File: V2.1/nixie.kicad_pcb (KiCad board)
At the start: 4 copper layers, 182.5 x 65.2 mm, 54 parts, among them IC1 SN74141, IC2 SN74141, IC3 SN74141, IC4 SN74141, IC5 MCP23017-E_SO, IC6 DS3231M+TRL, IC7 SN74141, IC8 SN74141, IC9 L7805CD2T-TR, J1 M20-9990446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

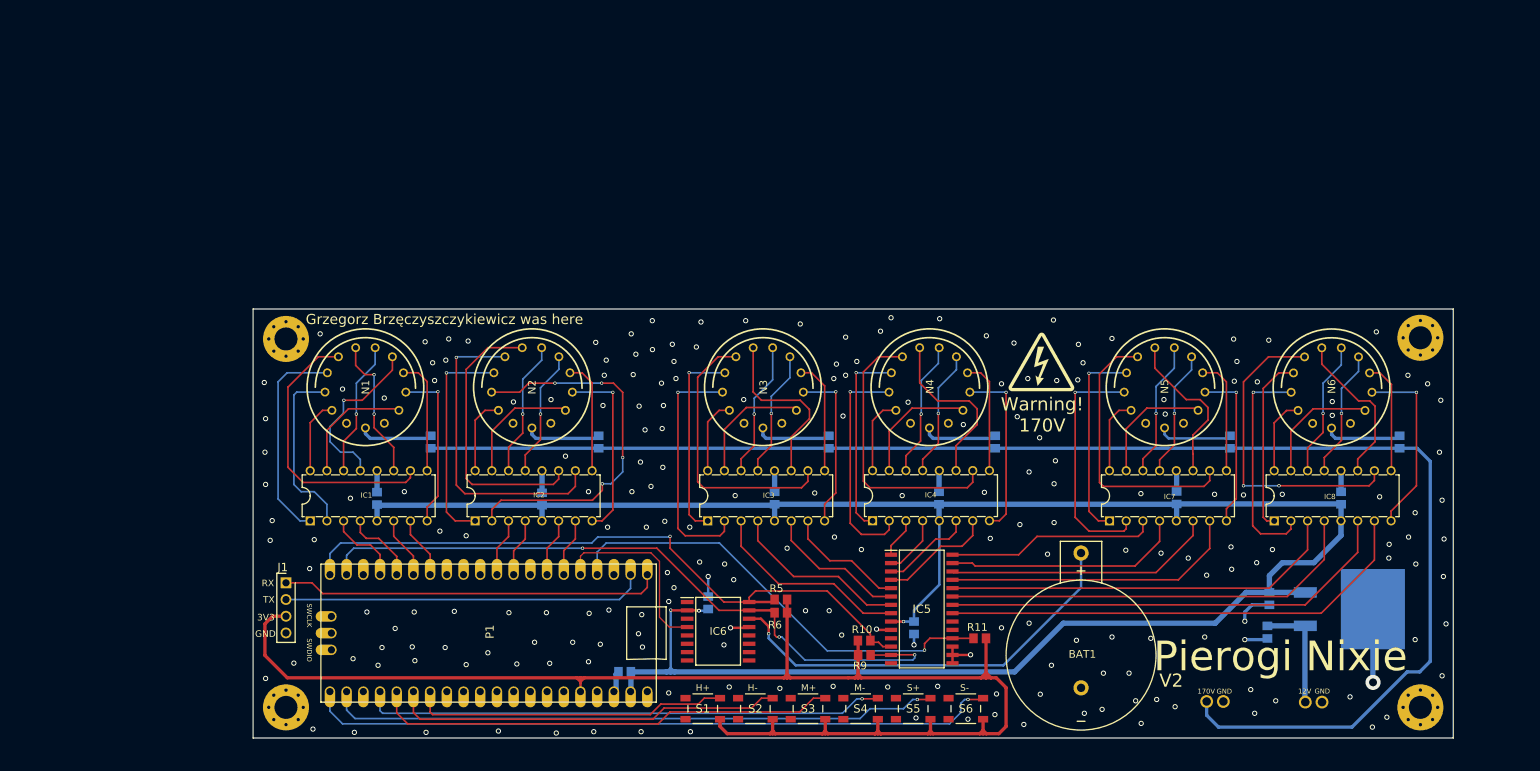
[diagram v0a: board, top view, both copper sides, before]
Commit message: Reorganizing Repo
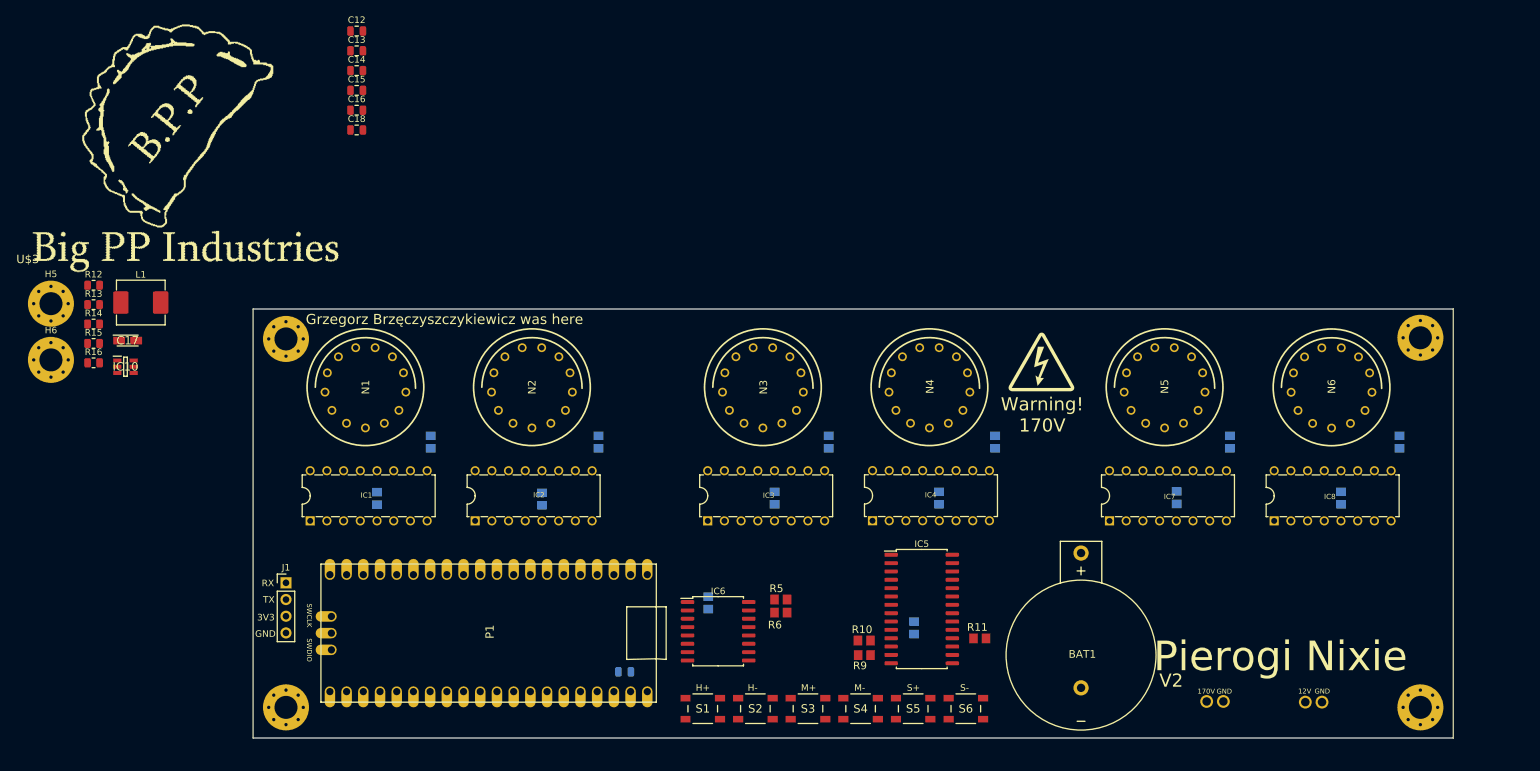
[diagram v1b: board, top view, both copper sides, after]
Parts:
- removed C10: .33uF, nixie:C0805
- removed C11: .1uF, nixie:C0805
- removed IC9: L7805CD2T-TR, footprints:L7805CD2T
- added C12: 10uF, Capacitor_SMD:C_0805_2012Metric, F.Cu at (80.8, 35.5)
- added C13: .1uF, Capacitor_SMD:C_0805_2012Metric, F.Cu at (80.8, 38.6)
- added C14: .1uF, Capacitor_SMD:C_0805_2012Metric, F.Cu at (80.8, 41.6)
- added C15: 22uF, Capacitor_SMD:C_0805_2012Metric, F.Cu at (80.8, 44.6)
- added C16: 22uF, Capacitor_SMD:C_0805_2012Metric, F.Cu at (80.8, 47.6)
- added C17: 47uF, footprints:CAPPM3216X180N, F.Cu at (45.9, 82.6)
- added C18: 75pF, Capacitor_SMD:C_0805_2012Metric, F.Cu at (80.8, 50.6)
- added H5: MountingHole, MountingHole:MountingHole_3.5mm_Pad_Via, F.Cu at (34.3, 77.0)
- added H6: MountingHole, MountingHole:MountingHole_3.5mm_Pad_Via, F.Cu at (34.3, 85.6)
- added IC10: TPS54302DDCT, footprints:SOT95P280X110-6N, F.Cu at (45.6, 86.6)
- added L1: 10uH, Inductor_SMD:L_Abracon_ASPI-0630LR, F.Cu at (47.9, 76.8)
- added R12: 511K, Resistor_SMD:R_0805_2012Metric, F.Cu at (40.7, 74.2)
- added R13: 105K, Resistor_SMD:R_0805_2012Metric, F.Cu at (40.7, 77.2)
- added R14: 49.9, Resistor_SMD:R_0805_2012Metric, F.Cu at (40.7, 80.1)
- added R15: 100K, Resistor_SMD:R_0805_2012Metric, F.Cu at (40.7, 83.1)
- added R16: 13.3K, Resistor_SMD:R_0805_2012Metric, F.Cu at (40.7, 86.0)
- added U$3: BIGPP, nixie:BIGPP, F.Cu at (30.7, 70.3)
- C6: footprint nixie:C0805 -> Capacitor_SMD:C_0805_2012Metric
- IC1, IC3, IC4, IC7, IC8: value SN74141 -> K155ID1
- IC5: footprint L7805CV:SOIC127P1030X265-28N -> Package_SO:SOIC-28W_7.5x17.9mm_P1.27mm
- IC6: footprint nixie:SOIC127P1032X265-16N -> Package_SO:SOIC-16W_7.5x10.3mm_P1.27mm
- J1: footprint footprints:HDRV4W64P0X254_1X4_1016X254X889P -> Connector_PinHeader_2.54mm:PinHeader_1x04_P2.54mm_Vertical
- turned J1 to 0 degrees
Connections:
- IC6 pad 10: unconnected-(IC6-N.C._6-Pad10) -> GND
- IC6 pad 11: unconnected-(IC6-N.C._7-Pad11) -> GND
- IC6 pad 12: unconnected-(IC6-N.C._8-Pad12) -> GND
- IC6 pad 14: Net-(IC6-VBAT) -> Net-(BAT1-+)
- IC6 pad 5: unconnected-(IC6-N.C._1-Pad5) -> GND
- IC6 pad 6: unconnected-(IC6-N.C._2-Pad6) -> GND
- IC6 pad 7: unconnected-(IC6-N.C._3-Pad7) -> GND
- IC6 pad 8: unconnected-(IC6-N.C._4-Pad8) -> GND
- IC6 pad 9: unconnected-(IC6-N.C._5-Pad9) -> GND
- J1 pad 1: /RX -> +3V3
- J1 pad 2: /TX -> /RX
- J1 pad 3: +3V3 -> /TX
- R1 pad 1: /170V1 -> VCC
- R1 pad 2: VCC -> /170V1
- R10 pad 1: /SCL1 -> +3V3
- R10 pad 2: +3V3 -> /SCL1
- R2 pad 1: /170V2 -> VCC
- R2 pad 2: VCC -> /170V2
- R3 pad 1: /170V3 -> VCC
- R3 pad 2: VCC -> /170V3
- R4 pad 1: /170V4 -> VCC
- R4 pad 2: VCC -> /170V4
- R5 pad 1: /SCL1 -> +3V3
- R5 pad 2: +3V3 -> /SCL1
- R9 pad 1: /SDA1 -> +3V3
- R9 pad 2: +3V3 -> /SDA1
- S3 pad 4: +3V3 -> unconnected-(S3-Pad4)
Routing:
- net +5V: track 327.9 -> 0.00 mm, vias 3 -> 0
- net +3V3: track 224.4 -> 0.00 mm
- net VCC: track 224.2 -> 0.00 mm
- net /SDA1: track 106.2 -> 0.00 mm, vias 3 -> 0
- net /S6: track 105.5 -> 0.00 mm, vias 1 -> 0
- net /SCL1: track 104.1 -> 0.00 mm, vias 1 -> 0
- net /S5: track 93.4 -> 0.00 mm, vias 1 -> 0
- net /S4: track 79.7 -> 0.00 mm, vias 1 -> 0
- net /C6: track 73.5 -> 0.00 mm
- net /S3: track 70.7 -> 0.00 mm
- net /B6: track 69.7 -> 0.00 mm
- net /RSTIO: track 69.4 -> 0.00 mm, vias 1 -> 0
- net /D6: track 64.7 -> 0.00 mm
- net Net-(IC6-VBAT): track 64.6 -> 0.00 mm, vias 1 -> 0
- net /A6: track 60.8 -> 0.00 mm
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
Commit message: Adjsuted more items in schematic, began layout
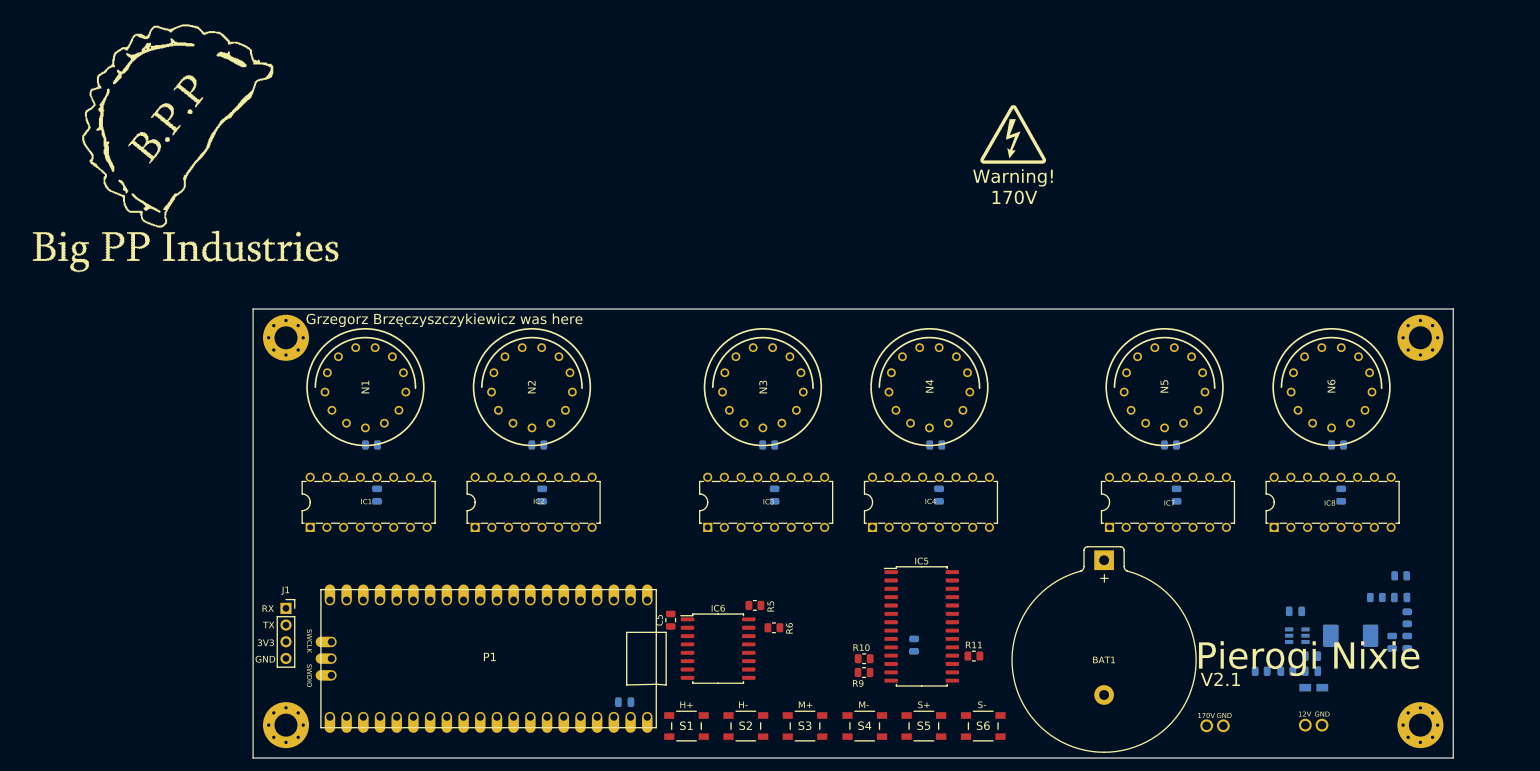
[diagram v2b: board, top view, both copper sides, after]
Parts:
- removed C17: 47uF, footprints:CAPPM3216X180N
- removed G***: LOGO, LOGO
- removed H5, H6: MountingHole, MountingHole:MountingHole_3.5mm_Pad_Via
- added C10: 47uF, footprints:CAPPM3216X180N, B.Cu at (226.3, 135.4)
- BAT1: value SN2032 -> 36-106-ND; footprint nixie:SN2032 -> Battery:BatteryHolder_Keystone_106_1x20mm
- C1, C2, C3, C4, C7, C8, C9: footprint nixie:C0805 -> Capacitor_SMD:C_0805_2012Metric
- C12, C13, C14, C15, C16, C18, IC10, L1, R12, R13, R14, R15, R16: moved to B.Cu
- C5: footprint nixie:C0805 -> Capacitor_SMD:C_0805_2012Metric; moved to F.Cu
- J1: footprint Connector_PinHeader_2.54mm:PinHeader_1x04_P2.54mm_Vertical -> Connector_PinSocket_2.54mm:PinSocket_1x04_P2.54mm_Vertical
- R1, R10, R11, R2, R3, R4, R5, R6, R7, R8, R9: footprint nixie:R0805 -> Resistor_SMD:R_0805_2012Metric
- moved R14 204.7 mm to (240.5, 124.8), turned to 90 degrees
- moved R15 201.9 mm to (239.5, 118.4), turned to 180 degrees
- moved R16 198.3 mm to (235.8, 121.7), turned to 180 degrees
- moved L1 190.8 mm to (231.9, 127.5)
- moved R12 190.7 mm to (222.2, 132.9), turned to 180 degrees
- moved R13 186.1 mm to (218.3, 132.9), turned to 180 degrees
- moved IC10 182.8 mm to (223.8, 127.5), turned to 180 degrees
- moved C16 179.1 mm to (240.5, 128.5), turned to -90 degrees
- moved C15 178.4 mm to (238.2, 128.5), turned to -90 degrees
- moved C12 174.8 mm to (225.9, 132.9)
- moved C18 173.9 mm to (239.5, 121.7), turned to 180 degrees
- moved C13 171.9 mm to (225.9, 130.6)
- moved C14 164.7 mm to (223.5, 123.8)
- moved U$2 34.9 mm to (175.5, 56.3)
- moved BAT1 14.8 mm to (194.4, 116.0), turned to -90 degrees
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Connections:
- S3 pad 4: unconnected-(S3-Pad4) -> +3V3
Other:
- board size 182.5 x 65.2 mm -> 182.5 x 68.3 mm
- board text added: "V2.1"
- board text removed: "V2"

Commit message: Started routing
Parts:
- added C11: 10uF, Capacitor_SMD:C_0805_2012Metric, B.Cu at (121.5, 135.4)
- C7: moved to F.Cu
- J1: footprint Connector_PinSocket_2.54mm:PinSocket_1x04_P2.54mm_Vertical -> Connector_PinHeader_2.54mm:PinHeader_1x04_P2.54mm_Vertical
- moved C7 7.66 mm to (157.9, 128.0), turned to 180 degrees
- moved C1 2.28 mm to (83.8, 108.4)
- moved C2 2.28 mm to (108.9, 108.4)
- moved C3 2.28 mm to (144.3, 108.4)
- moved C4 2.28 mm to (169.3, 108.4)
- moved C8 2.28 mm to (205.4, 108.4)
- moved C9 2.28 mm to (230.4, 108.4)
- moved BAT1 0.49 mm to (194.4, 116.5)
- moved J1 0.40 mm to (69.6, 123.3)
- moved C5 0.16 mm to (128.5, 125.3)
- moved L1 0.10 mm to (231.9, 127.6)
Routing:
- net +5V: track 0.00 -> 324.4 mm
- net VCC: track 0.00 -> 258.3 mm
- net +3V3: track 0.00 -> 164.4 mm
- net /S6: track 0.00 -> 115.2 mm, vias 0 -> 2
- net /SDA1: track 0.00 -> 101.6 mm, vias 0 -> 4
- net /S5: track 0.00 -> 97.9 mm, vias 0 -> 1
- net /S4: track 0.00 -> 83.3 mm, vias 0 -> 1
- net /S3: track 0.00 -> 71.2 mm, vias 0 -> 1
- net /SCL1: track 0.00 -> 70.5 mm
- net Net-(BAT1-+): track 0.00 -> 61.1 mm, vias 0 -> 1
- net /S2: track 0.00 -> 59.2 mm, vias 0 -> 1
- net GND: track 0.00 -> 55.4 mm, vias 0 -> 30
- net /S1: track 0.00 -> 46.3 mm, vias 0 -> 1
- net Net-(IC10-FB): track 0.00 -> 30.6 mm, vias 0 -> 2
- net /RSTC: track 0.00 -> 20.5 mm, vias 0 -> 1
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
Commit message: Continued routing
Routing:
- net /C6: track 0.00 -> 72.5 mm
- net /B6: track 0.00 -> 69.4 mm
- net +3V3: track 164.4 -> 228.5 mm, vias 0 -> 1
- net /D6: track 0.00 -> 63.7 mm
- net /A6: track 0.00 -> 60.5 mm
- net /RX: track 0.00 -> 57.8 mm, vias 0 -> 1
- net /TX: track 0.00 -> 57.3 mm, vias 0 -> 1
- net /C5: track 0.00 -> 47.9 mm
- net /B5: track 0.00 -> 43.5 mm
- net /D5: track 0.00 -> 39.5 mm
- net /A5: track 0.00 -> 35.5 mm
- net /A3: track 0.00 -> 31.3 mm
- net /D3: track 0.00 -> 27.8 mm
- net /B3: track 0.00 -> 22.5 mm
- net /C3: track 0.00 -> 19.4 mm
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
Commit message: continued routing
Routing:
- net /N17: track 0.00 -> 41.8 mm
- net /N27: track 0.00 -> 41.6 mm
- net /N16: track 0.00 -> 35.4 mm
- net /N26: track 0.00 -> 34.6 mm
- net /N29: track 0.00 -> 30.5 mm, vias 0 -> 2
- net /N22: track 0.00 -> 30.3 mm, vias 0 -> 1
- net /N19: track 0.00 -> 29.9 mm
- net /N24: track 0.00 -> 28.3 mm
- net /N18: track 0.00 -> 28.2 mm
- net /N14: track 0.00 -> 28.2 mm
- net /N28: track 0.00 -> 28.1 mm
- net /N12: track 0.00 -> 28.0 mm, vias 0 -> 1
- net /N23: track 0.00 -> 24.3 mm, vias 0 -> 1
- net /N13: track 0.00 -> 22.3 mm, vias 0 -> 1
- net /N25: track 0.00 -> 21.8 mm, vias 0 -> 1
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
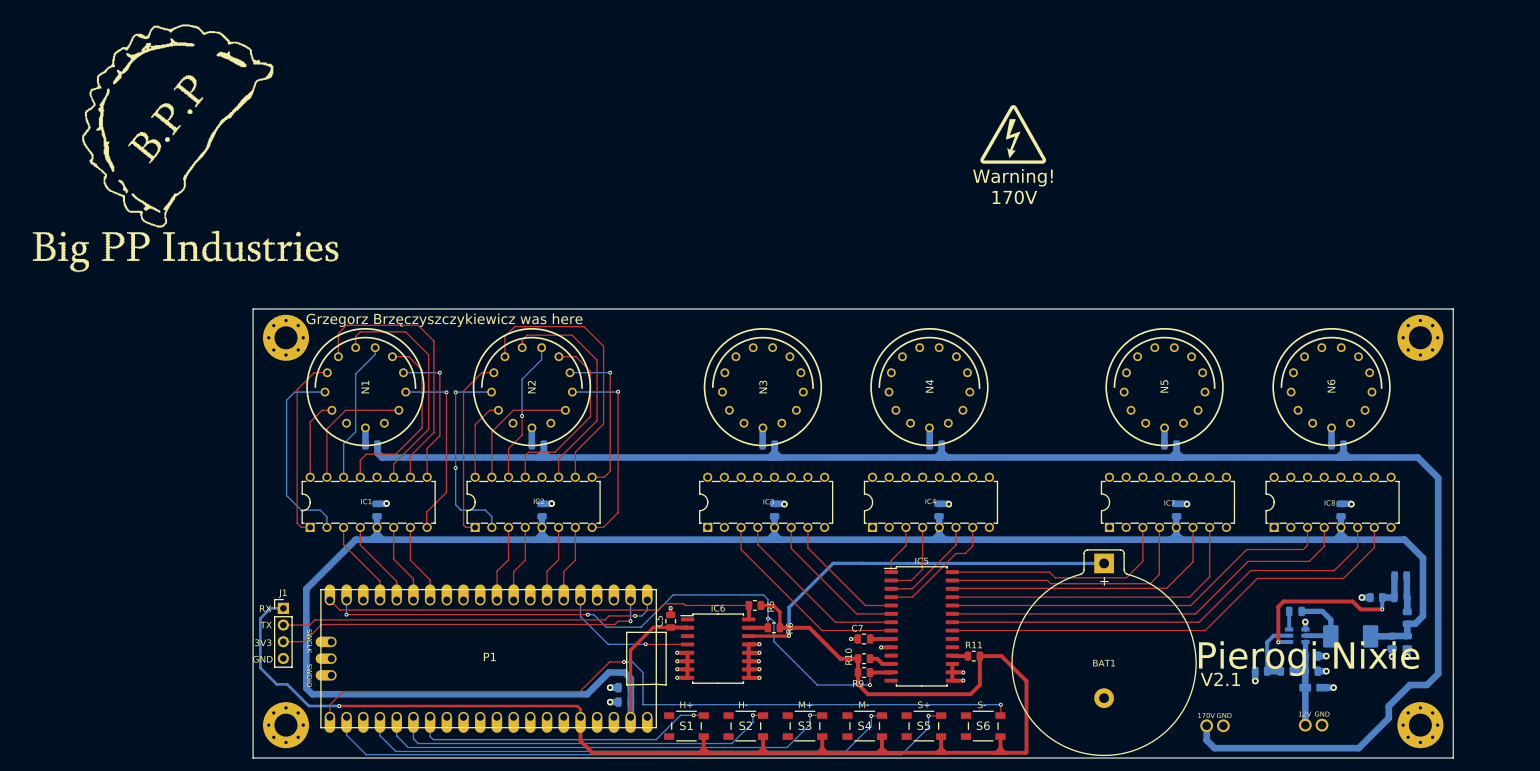
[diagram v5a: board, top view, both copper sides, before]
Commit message: Finished routing, added vias
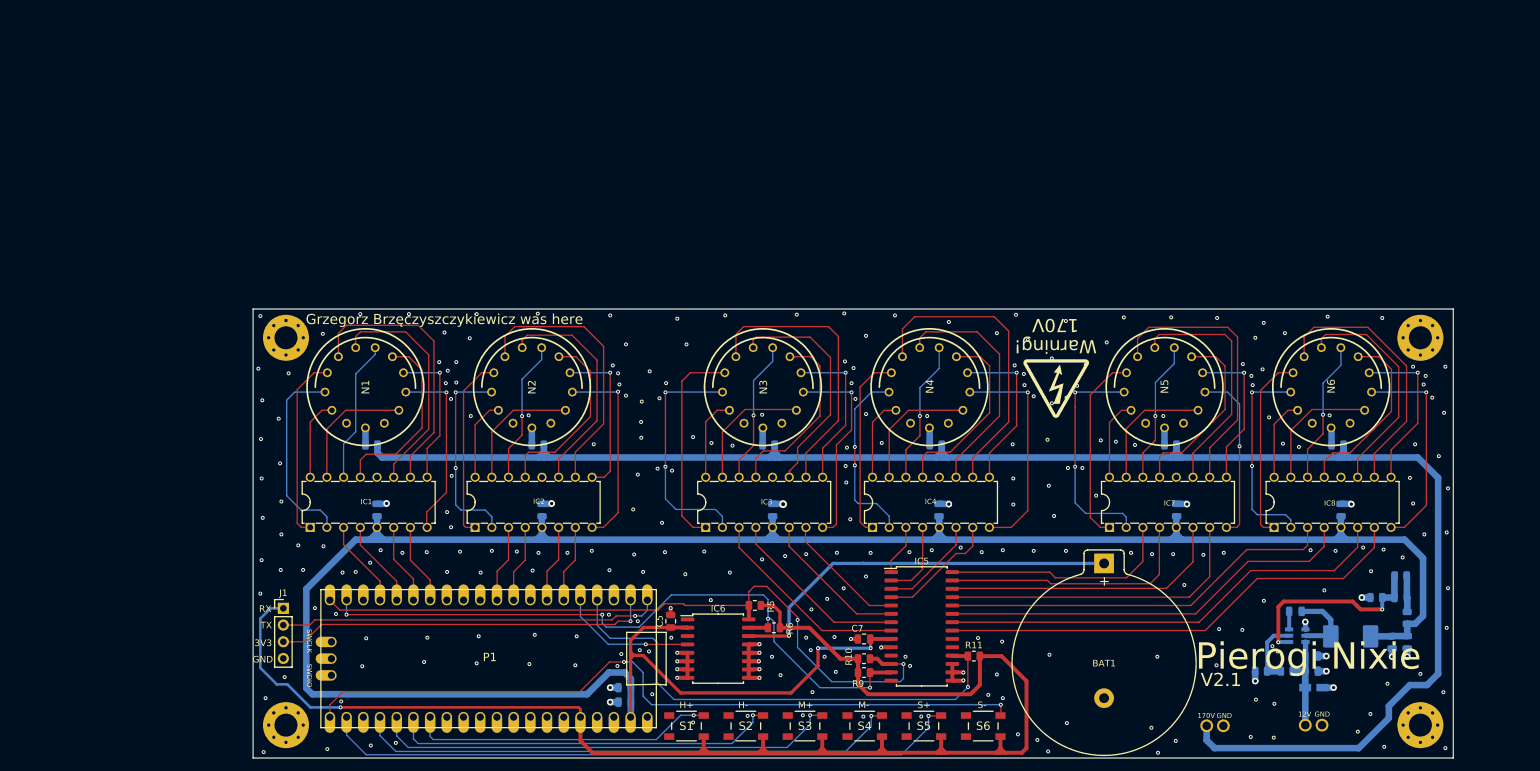
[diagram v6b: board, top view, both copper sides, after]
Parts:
- U$3: moved to B.Cu
- moved U$3 162.4 mm to (181.5, 130.7), turned to 180 degrees
- moved U$2 33.1 mm to (192.2, 84.9), turned to 180 degrees
- moved C3 0.30 mm to (144.0, 108.4)
- moved IC3 0.30 mm to (142.7, 107.2)
- moved N6 0.06 mm to (228.9, 89.7)
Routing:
- net /RSTIO: track 2.39 -> 76.3 mm, vias 0 -> 1
- net +5V: track 323.8 -> 371.6 mm, vias 0 -> 2
- net /N47: track 0.00 -> 46.5 mm
- net /N37: track 0.00 -> 43.6 mm
- net /N57: track 0.00 -> 42.4 mm
- net /N67: track 0.00 -> 40.6 mm
- net /SCL1: track 70.5 -> 109.4 mm, vias 0 -> 2
- net /N46: track 0.00 -> 36.8 mm
- net /N56: track 0.00 -> 36.8 mm
- net /N39: track 0.00 -> 36.3 mm, vias 0 -> 2
- net /N36: track 0.00 -> 35.2 mm
- net /N66: track 0.00 -> 34.8 mm
- net /N59: track 0.00 -> 34.5 mm, vias 0 -> 2
- net /N42: track 0.00 -> 33.7 mm, vias 0 -> 1
- net /N62: track 0.00 -> 32.3 mm, vias 0 -> 1
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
